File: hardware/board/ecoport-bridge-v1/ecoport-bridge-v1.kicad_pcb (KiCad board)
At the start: 2 copper layers, 51.5 x 92 mm, 68 parts, among them J1 420B2V12FL0, J2 Conn_01x02, J3 SM04B-SRSS-TB, J4 USB4085-GF-A, J5 Conn_01x02, J6 Connector Wire, J7 B3B-PH-K-S, SW1 RESET, SW2 BOOT, U1 IRM-05-5, U2 TLV75733PDBVR, U3 SP3485EET, U4 USBLC6-2SC6, U5 SN74LV1T34DCKR, U6 ESP32-C6-WROOM-1-N8, U7 USBLC6-2SC6

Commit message: Added fuse
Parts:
- added F1: SF-2410SP050W-2, Samacsys:FUSC6125X236N, F.Cu at (72.5, 46.4)
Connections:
- U1 pad 1: /AC_L2 -> /AC_L2_F
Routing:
- net /AC_L2: track 12.6 -> 4.31 mm
- net /AC_L2_F: track 0.00 -> 6.34 mm
- net /AC_L1: track 22.5 -> 21.7 mm

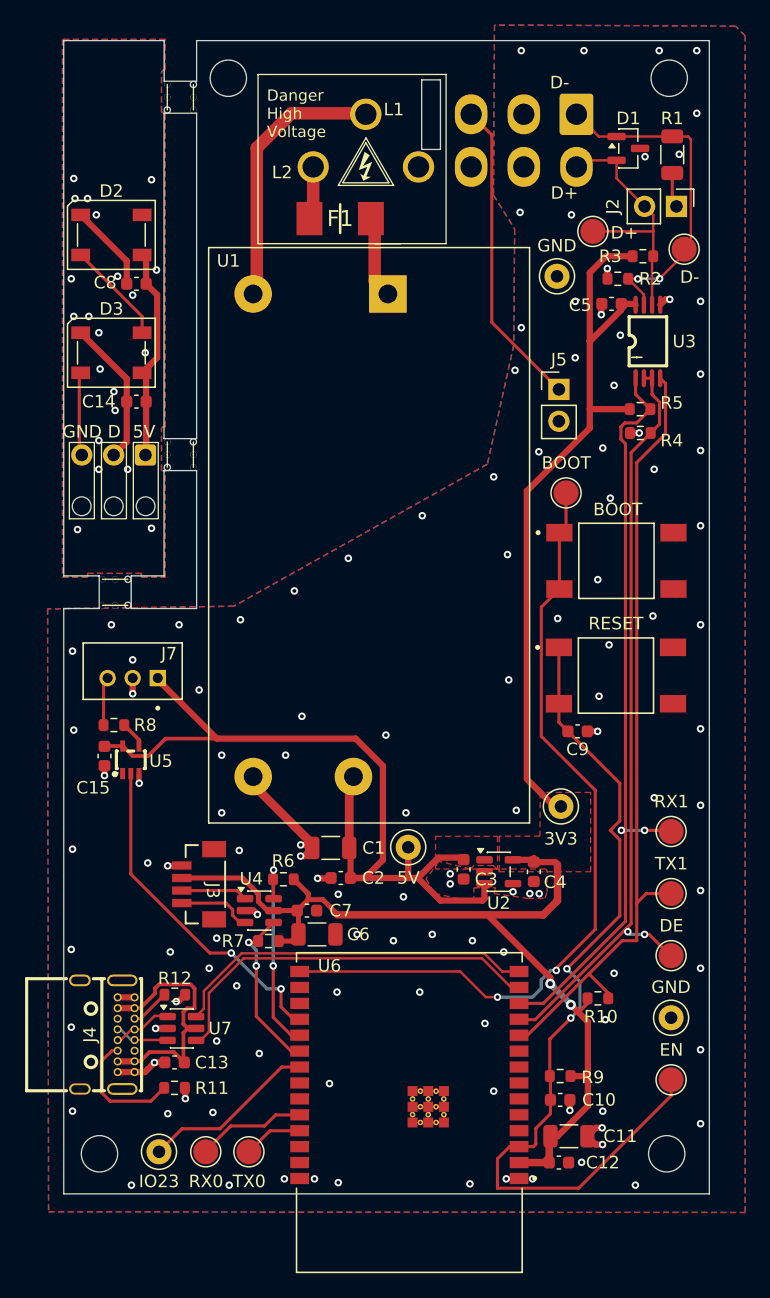
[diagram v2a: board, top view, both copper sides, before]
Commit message: added usb power and reorganized assets
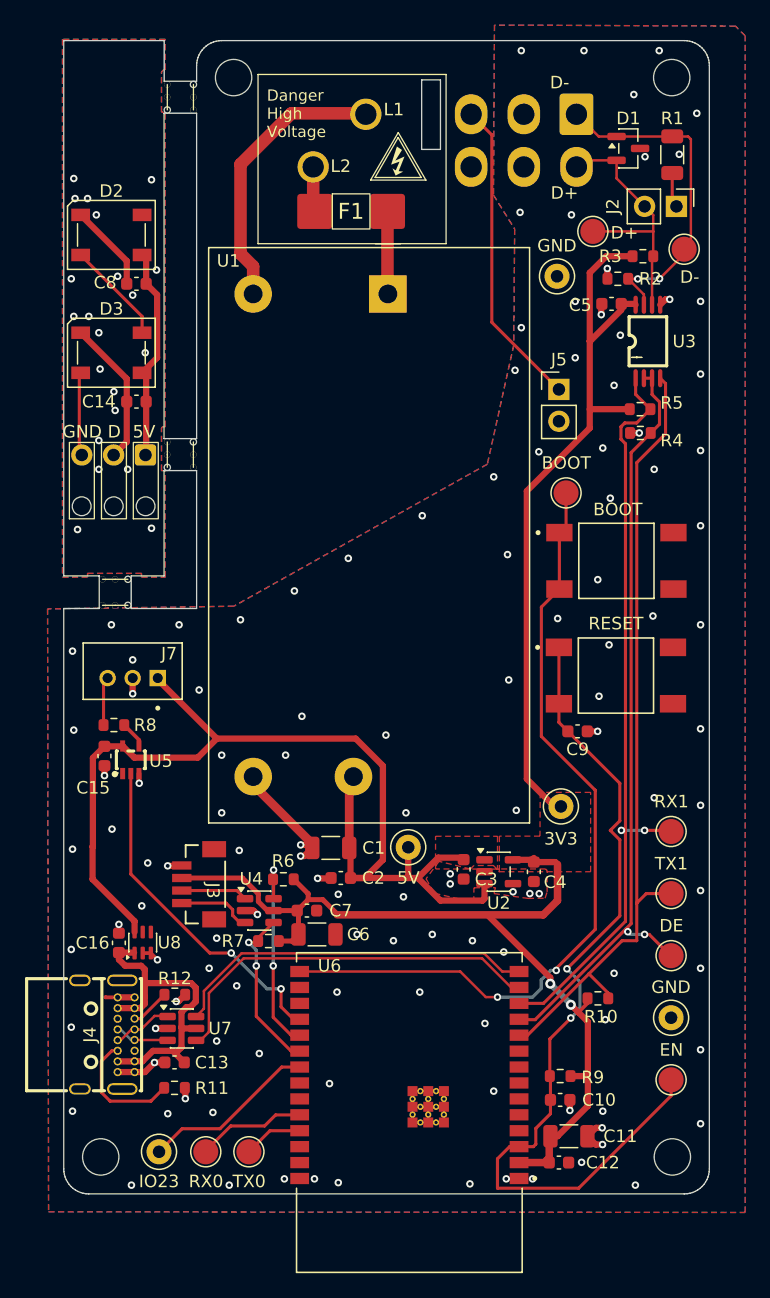
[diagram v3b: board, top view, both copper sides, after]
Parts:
- added C16: 1µF, Capacitor_SMD:C_0603_1608Metric, F.Cu at (54.9, 104.2)
- added U8: LM66100DCKR, Package_TO_SOT_SMD:SOT-363_SC-70-6, F.Cu at (56.8, 104.2)
- F1: footprint Samacsys:FUSC6125X236N -> Custom:FUSC6125X236N
- J7: footprint Snapeda:JST_B3B-PH-K-S -> Custom:JST_B3B-PH-K-S
- SW1, SW2: footprint Snapeda:SW_TS04-66-50-BK-260-SMT -> Custom:SW_TS04-66-50-BK-260-SMT
- U3: footprint EasyEDA:TSSOP-8_L4.4-W3.0-P0.65-LS6.4-BL -> Custom:TSSOP-8_L4.4-W3.0-P0.65-LS6.4-BL
- U5: footprint EasyEDA:SC-70-5_L2.1-W1.3-P0.65-LS2.1-BR -> Custom:SC-70-5_L2.1-W1.3-P0.65-LS2.1-BR
- moved G*** 2.61 mm to (77.2, 41.5)
- moved F1 1.04 mm to (73.4, 45.8)
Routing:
- net +5V: track 69.4 -> 86.1 mm
- net VBUS: track 21.4 -> 26.9 mm
- net GND: track 31.9 -> 34.3 mm, vias 120 -> 123
- net /AC_L1: track 21.7 -> 22.5 mm
- net /AC_L2: track 4.31 -> 3.60 mm
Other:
- outline, holes or cut-outs redrawn
